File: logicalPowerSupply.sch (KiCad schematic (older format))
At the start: 12 parts

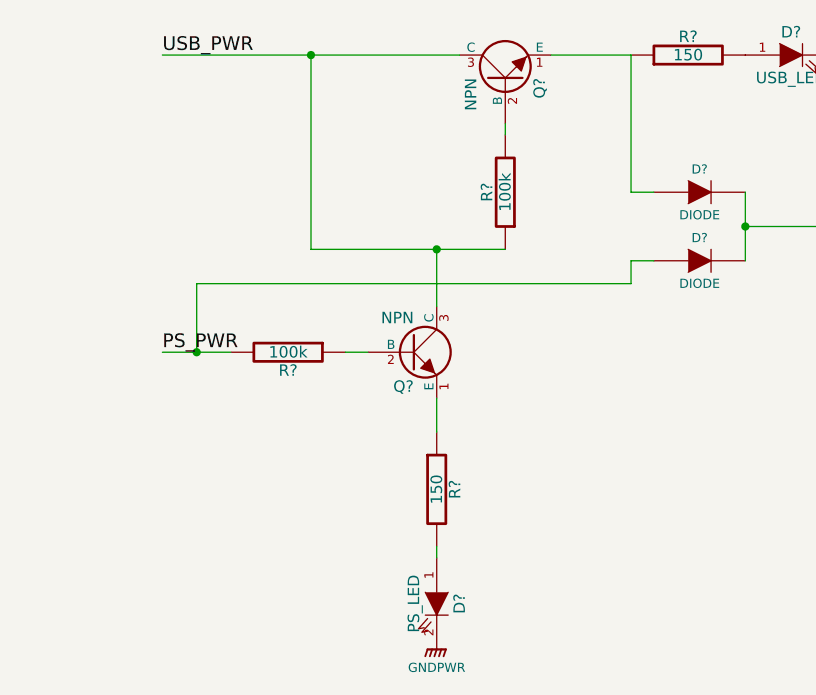
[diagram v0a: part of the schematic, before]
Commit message: Updating the logic circuit for the power supply
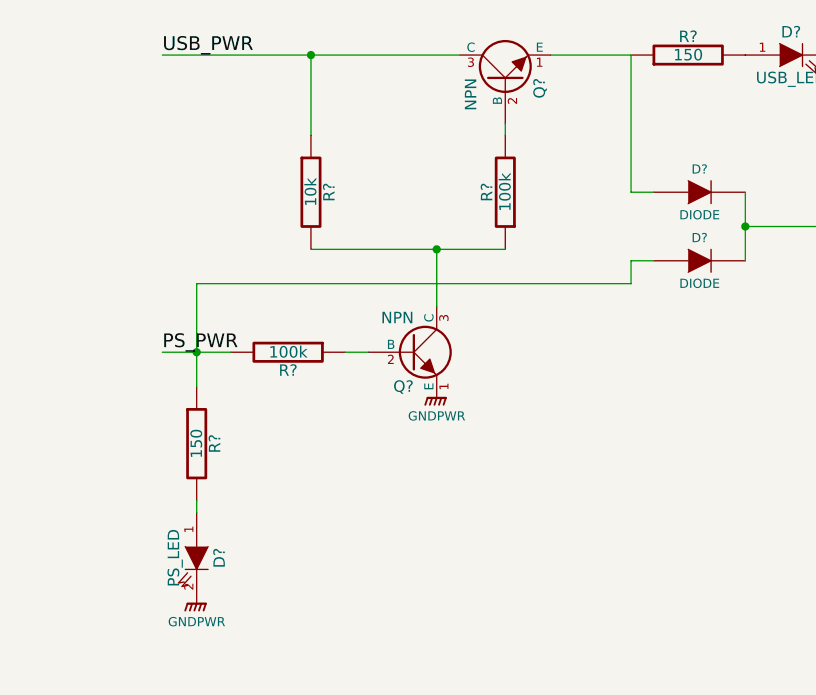
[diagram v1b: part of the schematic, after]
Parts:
- added R?: 10k, symbol R
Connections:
- net GNDPWR: now also Q?.1 (E)
- net PS_PWR: now also R?.1
- net USB_PWR: now also R?.1; no longer Q?.3 (C), R?.1
- new net: Q?.3 (C), R?.1, R?.2
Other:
- moved on the sheet: D?, R?
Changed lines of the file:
@@
-EESchema Schematic File Version 2  date 9/10/2011 2:20:11 AM
+EESchema Schematic File Version 2  date 9/12/2011 9:56:45 PM
 LIBS:power
 LIBS:device
@@
 LIBS:contrib
 LIBS:valves
+LIBS:logicalPowerSupply-cache
 EELAYER 25  0
 EELAYER END
@@
 Sheet 1 1
 Title ""
-Date "10 sep 2011"
+Date "13 sep 2011"
 Rev ""
 Comp ""
@@
 $Comp
 L GNDPWR #PWR?
+U 1 1 4E6EC664
+P 4050 2700
+F 0 "#PWR?" H 4050 2750 40  0001 C CNN
+F 1 "GNDPWR" H 4050 2620 40  0000 C CNN
+	1    4050 2700
+	1    0    0    -1
+$EndComp
+Wire Wire Line
+	3500 1200 3500 1550
+Connection ~ 3500 1200
+Wire Wire Line
+	2850 1200 4150 1200
+Wire Wire Line
+	5400 1800 5400 2100
+Wire Wire Line
+	5000 2100 4900 2100
+Wire Wire Line
+	3000 2200 4900 2200
+Connection ~ 3000 2500
+Wire Wire Line
+	3000 2200 3000 2500
+Wire Wire Line
+	2850 2500 3150 2500
+Wire Wire Line
+	4350 2050 3500 2050
+Wire Wire Line
+	3650 2500 3750 2500
+Wire Wire Line
+	4350 1500 4350 1550
+Wire Wire Line
+	4050 2300 4050 2050
+Connection ~ 4050 2050
+Wire Wire Line
+	4550 1200 4900 1200
+Wire Wire Line
+	4900 1200 4900 1800
+Wire Wire Line
+	4900 1800 5000 1800
+Wire Wire Line
+	4900 2200 4900 2100
+Wire Wire Line
+	5400 1950 6000 1950
+Connection ~ 5400 1950
+Wire Wire Line
+	3000 2650 3000 2500
+Wire Wire Line
+	3000 3150 3000 3200
+$Comp
+L R R?
+U 1 1 4E6EC640
+P 3500 1800
+F 0 "R?" V 3580 1800 50  0000 C CNN
+F 1 "10k" V 3500 1800 50  0000 C CNN
+	1    3500 1800
+	1    0    0    -1
+$EndComp
+$Comp
+L GNDPWR #PWR?
 U 1 1 4E6B0F6E
 P 5800 1200
@@
 	0    -1   -1   0
 $EndComp
-Wire Wire Line
-	4050 3350 4050 3400
-Wire Wire Line
-	4050 2850 4050 2700
-Connection ~ 5400 1950
-Wire Wire Line
-	5400 1950 6000 1950
-Wire Wire Line
-	4900 2200 4900 2100
-Wire Wire Line
-	5000 1800 4900 1800
-Wire Wire Line
-	4900 1800 4900 1200
-Wire Wire Line
-	4900 1200 4550 1200
-Connection ~ 4050 2050
-Wire Wire Line
-	4050 2300 4050 2050
-Wire Wire Line
-	4350 1500 4350 1550
-Wire Wire Line
-	3650 2500 3750 2500
-Wire Wire Line
-	4350 2050 3500 2050
-Wire Wire Line
-	2850 2500 3150 2500
-Wire Wire Line
-	3000 2500 3000 2200
-Connection ~ 3000 2500
-Wire Wire Line
-	3000 2200 4900 2200
-Wire Wire Line
-	4900 2100 5000 2100
-Wire Wire Line
-	5400 1800 5400 2100
-Wire Wire Line
-	2850 1200 4150 1200
-Connection ~ 3500 1200
-Wire Wire Line
-	3500 2050 3500 1200
 $Comp
 L LED D?
 U 1 1 4E6B0ED4
-P 4050 3600
-F 0 "D?" H 4050 3700 50  0000 C CNN
-F 1 "PS_LED" H 4050 3500 50  0000 C CNN
-	1    4050 3600
+P 3000 3400
+F 0 "D?" H 3000 3500 50  0000 C CNN
+F 1 "PS_LED" H 3000 3300 50  0000 C CNN
+	1    3000 3400
 	0    1    1    0
 $EndComp
@@
 L GNDPWR #PWR?
 U 1 1 4E6B01CF
-P 4050 3800
-F 0 "#PWR?" H 4050 3850 40  0001 C CNN
-F 1 "GNDPWR" H 4050 3720 40  0000 C CNN
-	1    4050 3800
+P 3000 3600
+F 0 "#PWR?" H 3000 3650 40  0001 C CNN
+F 1 "GNDPWR" H 3000 3520 40  0000 C CNN
+	1    3000 3600
 	1    0    0    -1
 $EndComp
@@
 L R R?
 U 1 1 4E6B0012
-P 4050 3100
-F 0 "R?" V 4130 3100 50  0000 C CNN
-F 1 "150" V 4050 3100 50  0000 C CNN
-	1    4050 3100
-	1    0    0    -1
-$EndComp
+P 3000 2900
+F 0 "R?" V 3080 2900 50  0000 C CNN
+F 1 "150" V 3000 2900 50  0000 C CNN
+	1    3000 2900
+	1    0    0    -1
+$EndComp

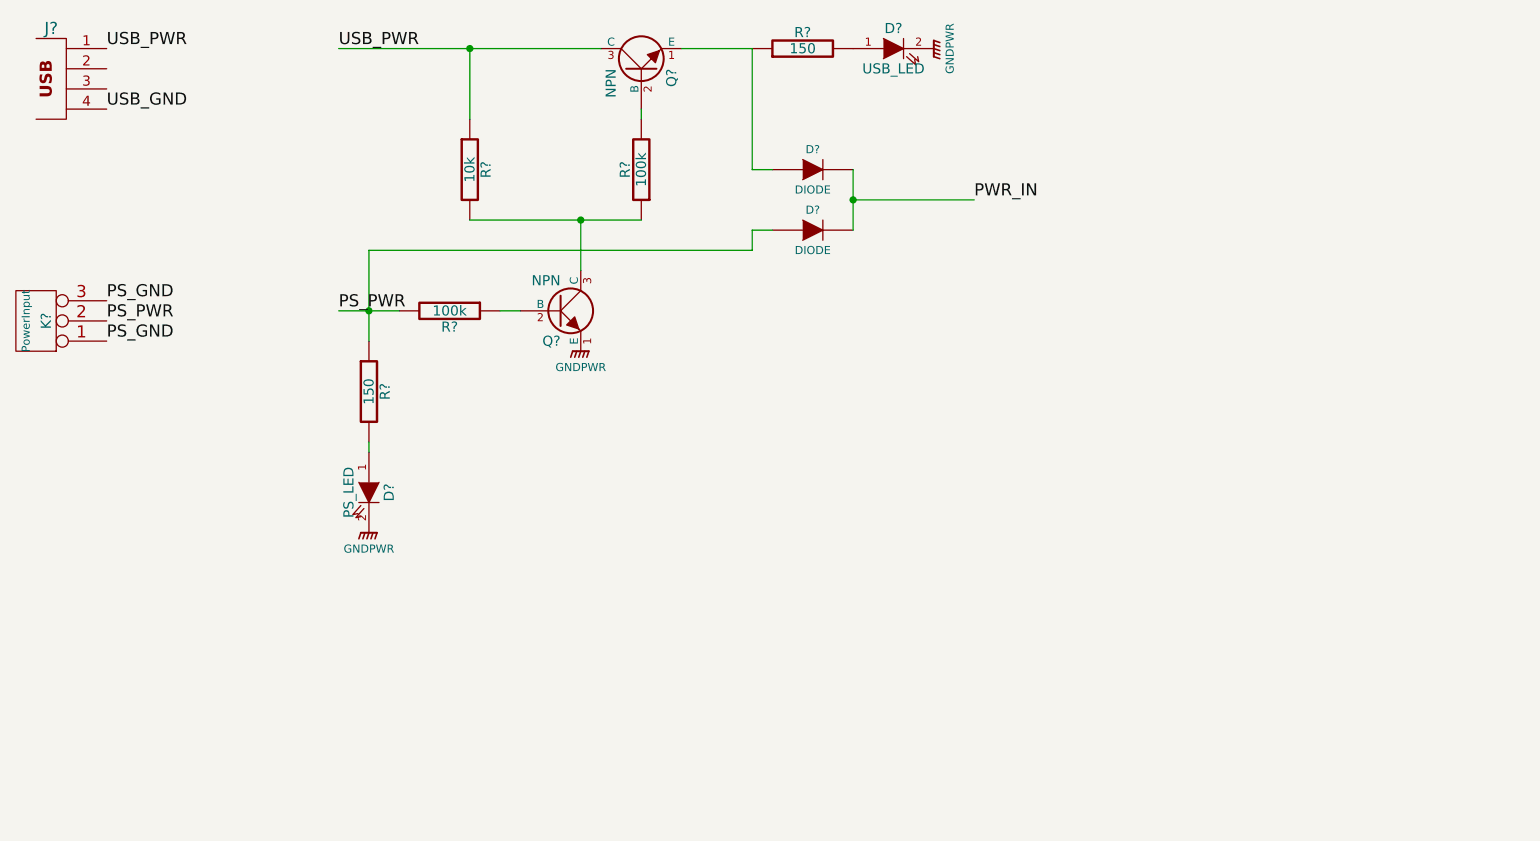
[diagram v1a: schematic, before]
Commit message: Added 3.3V switching Vreg to logPS schematic. Still need to settle on exact external components.
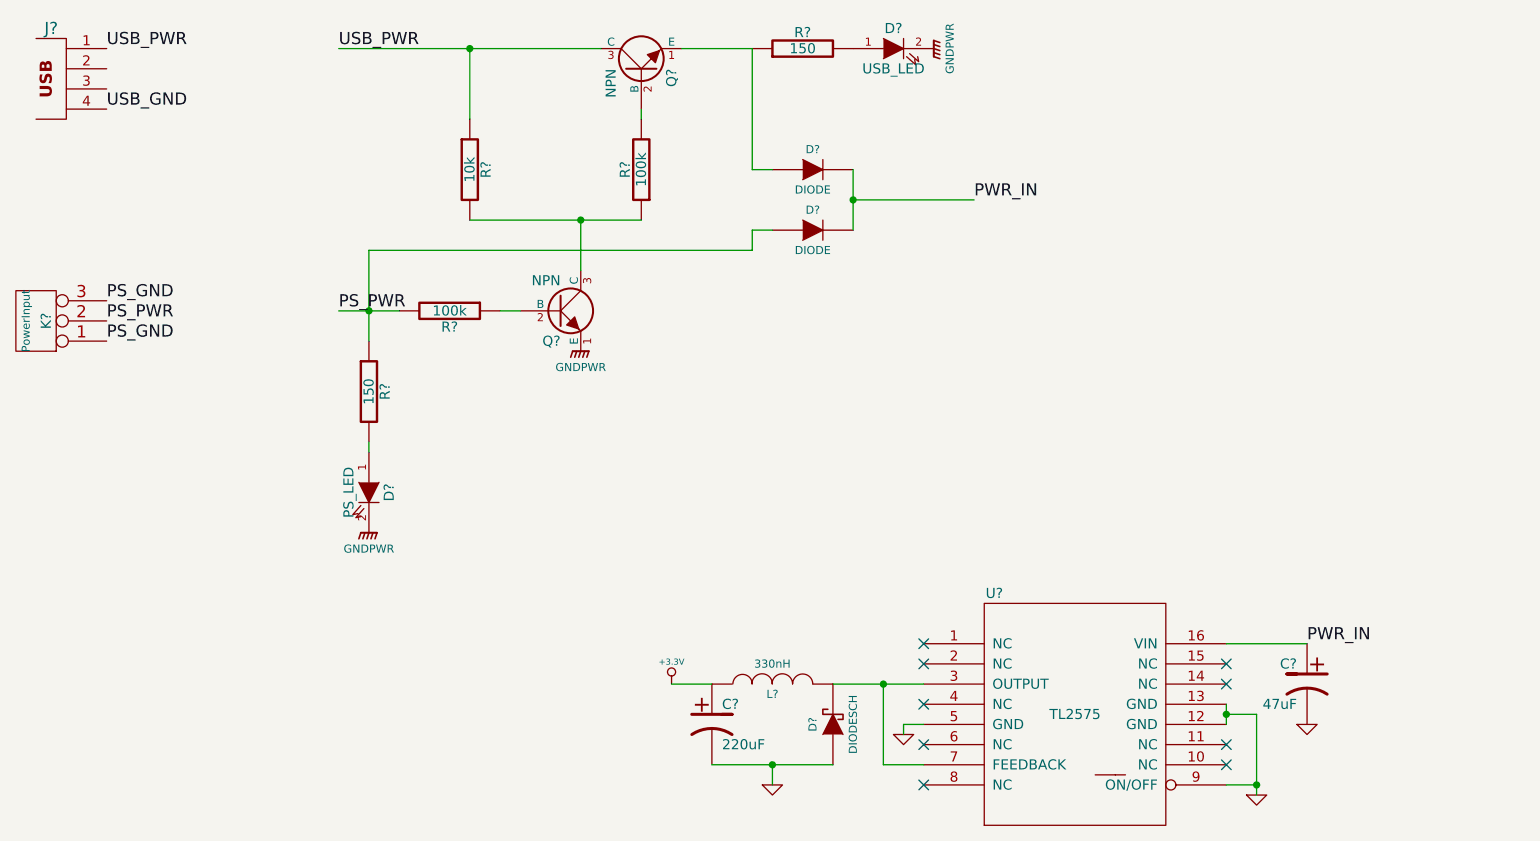
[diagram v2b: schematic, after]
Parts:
- added C?: 47uF, symbol CP1
- added C?: 220uF, symbol CP1
- added D?: DIODESCH, symbol DIODESCH
- added L?: 330nH, symbol INDUCTOR
- added U?: TL2575, symbol TL2575
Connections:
- net PWR_IN: now also C?.1, U?.16 (VIN)
- new net: D?.2 (K), L?.2, U?.3 (OUTPUT), U?.7 (FEEDBACK)
- new net +3.3V: C?.1, L?.1
- new net GND: C?.2, C?.2, D?.1 (A), U?.12 (GND), U?.13 (GND), U?.5 (GND), U?.9 (ON/OFF)
- no-connect marks 0 -> 9
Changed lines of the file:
@@
-EESchema Schematic File Version 2  date 9/12/2011 9:56:45 PM
+EESchema Schematic File Version 2  date 9/17/2011 1:18:32 AM
 LIBS:power
 LIBS:device
@@
 LIBS:contrib
 LIBS:valves
+LIBS:rrae
 LIBS:logicalPowerSupply-cache
 EELAYER 25  0
@@
 Sheet 1 1
 Title ""
-Date "13 sep 2011"
+Date "17 sep 2011"
 Rev ""
 Comp ""
@@
 Comment4 ""
 $EndDescr
+Wire Wire Line
+	4700 4350 4500 4350
+Wire Wire Line
+	5000 4850 5000 4750
+Connection ~ 5000 4750
+Wire Wire Line
+	7650 4150 7250 4150
+Connection ~ 7250 4500
+Wire Wire Line
+	7400 4900 7400 4500
+Wire Wire Line
+	7400 4500 7250 4500
+Wire Wire Line
+	5300 4350 5750 4350
+Wire Wire Line
+	7250 4450 7250 4550
+Wire Wire Line
+	3500 1200 3500 1550
+Connection ~ 3500 1200
+Wire Wire Line
+	2850 1200 4150 1200
+Wire Wire Line
+	5400 1800 5400 2100
+Wire Wire Line
+	5000 2100 4900 2100
+Wire Wire Line
+	4900 2200 3000 2200
+Connection ~ 3000 2500
+Wire Wire Line
+	2850 2500 3150 2500
+Wire Wire Line
+	4350 2050 3500 2050
+Wire Wire Line
+	3650 2500 3750 2500
+Wire Wire Line
+	4350 1500 4350 1550
+Wire Wire Line
+	4050 2300 4050 2050
+Connection ~ 4050 2050
+Wire Wire Line
+	4550 1200 4900 1200
+Wire Wire Line
+	4900 1200 4900 1800
+Wire Wire Line
+	4900 1800 5000 1800
+Wire Wire Line
+	4900 2200 4900 2100
+Wire Wire Line
+	5400 1950 6000 1950
+Connection ~ 5400 1950
+Wire Wire Line
+	3000 2200 3000 2650
+Wire Wire Line
+	3000 3150 3000 3200
+Wire Wire Line
+	5750 4550 5650 4550
+Wire Wire Line
+	5650 4550 5650 4600
+Wire Wire Line
+	5750 4750 5550 4750
+Wire Wire Line
+	5550 4750 5550 4350
+Connection ~ 5550 4350
+Wire Wire Line
+	7250 4850 7400 4850
+Connection ~ 7400 4850
+Wire Wire Line
+	5300 4750 4700 4750
+$Comp
+L GND #PWR?
+U 1 1 4E743AA5
+P 5000 4850
+F 0 "#PWR?" H 5000 4850 30  0001 C CNN
+F 1 "GND" H 5000 4780 30  0001 C CNN
+	1    5000 4850
+	1    0    0    -1
+$EndComp
+$Comp
+L INDUCTOR L?
+U 1 1 4E7439DF
+P 5000 4350
+F 0 "L?" V 4950 4350 40  0000 C CNN
+F 1 "330nH" V 5100 4350 40  0000 C CNN
+F 4 "Digi-Key" H 5000 4350 60  0001 C CNN "Supplier"
+F 5 "PCD1435CT-ND" H 5000 4350 60  0001 C CNN "PN"
+	1    5000 4350
+	0    -1   -1   0
+$EndComp
+$Comp
+L DIODESCH D?
+U 1 1 4E7437C8
+P 5300 4550
+F 0 "D?" H 5300 4650 40  0000 C CNN
+F 1 "DIODESCH" H 5300 4450 40  0000 C CNN
+F 4 "Digi-Key" H 5300 4550 60  0001 C CNN "Supplier"
+F 5 "568-4117-1-ND" H 5300 4550 60  0001 C CNN "PN"
+	1    5300 4550
+	0    -1   -1   0
+$EndComp
+$Comp
+L CP1 C?
+U 1 1 4E7435F7
+P 4700 4550
+F 0 "C?" H 4750 4650 50  0000 L CNN
+F 1 "220uF" H 4750 4450 50  0000 L CNN
+F 4 "Digi-Key" H 4700 4550 60  0001 C CNN "Supplier"
+F 5 "P5112-ND" H 4700 4550 60  0001 C CNN "PN"
+	1    4700 4550
+	1    0    0    -1
+$EndComp
+$Comp
+L GND #PWR?
+U 1 1 4E743381
+P 7650 4550
+F 0 "#PWR?" H 7650 4550 30  0001 C CNN
+F 1 "GND" H 7650 4480 30  0001 C CNN
+	1    7650 4550
+	1    0    0    -1
+$EndComp
+Text Label 7650 4150 0    60   ~ 0
+PWR_IN
+$Comp
+L CP1 C?
+U 1 1 4E7432CB
+P 7650 4350
+F 0 "C?" H 7700 4450 50  0000 L CNN
+F 1 "47uF" H 7700 4250 50  0000 L CNN
+F 4 "Digi-Key" H 7650 4350 60  0001 C CNN "Supplier"
+F 5 "493-1896-ND" H 7650 4350 60  0001 C CNN "PN"
+	1    7650 4350
+	-1   0    0    -1
+$EndComp
+$Comp
+L GND #PWR?
+U 1 1 4E742FEE
+P 5650 4600
+F 0 "#PWR?" H 5650 4600 30  0001 C CNN
+F 1 "GND" H 5650 4530 30  0001 C CNN
+	1    5650 4600
+	1    0    0    -1
+$EndComp
+$Comp
+L GND #PWR?
+U 1 1 4E742F8B
+P 7400 4900
+F 0 "#PWR?" H 7400 4900 30  0001 C CNN
+F 1 "GND" H 7400 4830 30  0001 C CNN
+	1    7400 4900
+	1    0    0    -1
+$EndComp
+$Comp
+L +3.3V #PWR?
+U 1 1 4E742F09
+P 4500 4350
+F 0 "#PWR?" H 4500 4310 30  0001 C CNN
+F 1 "+3.3V" H 4500 4460 30  0000 C CNN
+	1    4500 4350
+	1    0    0    -1
+$EndComp
+NoConn ~ 5750 4150
+NoConn ~ 5750 4250
+NoConn ~ 5750 4450
+NoConn ~ 5750 4650
+NoConn ~ 5750 4850
+NoConn ~ 7250 4750
+NoConn ~ 7250 4650
+NoConn ~ 7250 4350
+NoConn ~ 7250 4250
+$Comp
+L TL2575 U?
+U 1 1 4E742E92
+P 6500 4500
+F 0 "U?" H 6100 5100 50  0000 C CNN
+F 1 "TL2575" H 6500 4500 50  0000 C CNN
+	1    6500 4500
+	1    0    0    -1
+$EndComp
 $Comp
 L GNDPWR #PWR?
@@
 	1    0    0    -1
 $EndComp
-Wire Wire Line
-	3500 1200 3500 1550
-Connection ~ 3500 1200
-Wire Wire Line
-	2850 1200 4150 1200
-Wire Wire Line
-	5400 1800 5400 2100
-Wire Wire Line
-	5000 2100 4900 2100
-Wire Wire Line
-	3000 2200 4900 2200
-Connection ~ 3000 2500
-Wire Wire Line
-	3000 2200 3000 2500
-Wire Wire Line
-	2850 2500 3150 2500
-Wire Wire Line
-	4350 2050 3500 2050
-Wire Wire Line
-	3650 2500 3750 2500
-Wire Wire Line
-	4350 1500 4350 1550
-Wire Wire Line
-	4050 2300 4050 2050
-Connection ~ 4050 2050
-Wire Wire Line
-	4550 1200 4900 1200
-Wire Wire Line
-	4900 1200 4900 1800
-Wire Wire Line
-	4900 1800 5000 1800
-Wire Wire Line
-	4900 2200 4900 2100
-Wire Wire Line
-	5400 1950 6000 1950
-Connection ~ 5400 1950
-Wire Wire Line
-	3000 2650 3000 2500
-Wire Wire Line
-	3000 3150 3000 3200
 $Comp
 L R R?

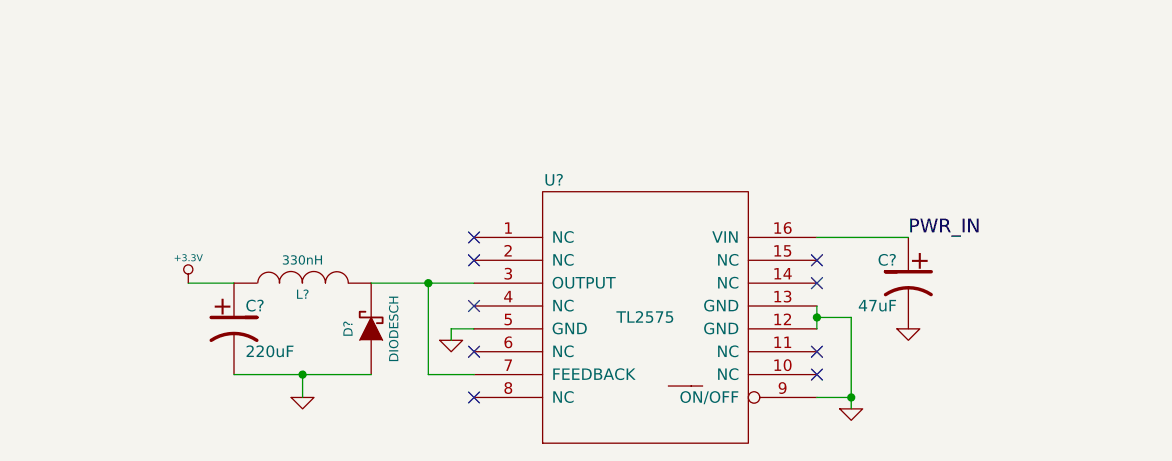
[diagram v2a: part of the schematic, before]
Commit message: Updated/corrected passive component values and product numbers per the TL2575 datasheet.
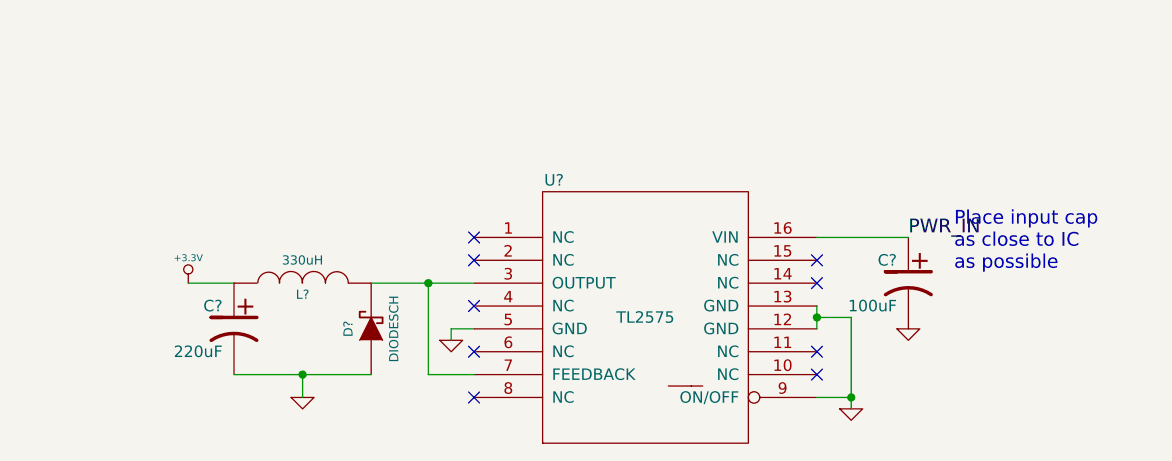
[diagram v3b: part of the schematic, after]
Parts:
- C?: value 47uF -> 100uF; PN 493-1896-ND -> P5165-ND
- D?: PN 568-4117-1-ND -> B340A-FDICT-ND
- L?: value 330nH -> 330uH; PN PCD1435CT-ND -> SRR1260-331KCT-ND
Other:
- note added: "Place input cap \nas close to IC \nas possible"
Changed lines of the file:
@@
-EESchema Schematic File Version 2  date 9/17/2011 1:18:32 AM
+EESchema Schematic File Version 2  date 9/20/2011 9:07:33 PM
 LIBS:power
 LIBS:device
@@
 LIBS:contrib
 LIBS:valves
-LIBS:rrae
 LIBS:logicalPowerSupply-cache
 EELAYER 25  0
@@
 Sheet 1 1
 Title ""
-Date "17 sep 2011"
+Date "21 sep 2011"
 Rev ""
 Comp ""
@@
 Comment4 ""
 $EndDescr
+Text Notes 7850 4300 0    60   ~ 0
+Place input cap \nas close to IC \nas possible
 Wire Wire Line
 	4700 4350 4500 4350
@@
 P 5000 4350
 F 0 "L?" V 4950 4350 40  0000 C CNN
-F 1 "330nH" V 5100 4350 40  0000 C CNN
+F 1 "330uH" V 5100 4350 40  0000 C CNN
 F 4 "Digi-Key" H 5000 4350 60  0001 C CNN "Supplier"
-F 5 "PCD1435CT-ND" H 5000 4350 60  0001 C CNN "PN"
+F 5 "SRR1260-331KCT-ND" H 5000 4350 60  0001 C CNN "PN"
 	1    5000 4350
 	0    -1   -1   0
@@
 F 1 "DIODESCH" H 5300 4450 40  0000 C CNN
 F 4 "Digi-Key" H 5300 4550 60  0001 C CNN "Supplier"
-F 5 "568-4117-1-ND" H 5300 4550 60  0001 C CNN "PN"
+F 5 "B340A-FDICT-ND" H 5300 4550 60  0001 C CNN "PN"
 	1    5300 4550
 	0    -1   -1   0
@@
 F 5 "P5112-ND" H 4700 4550 60  0001 C CNN "PN"
 	1    4700 4550
-	1    0    0    -1
+	-1   0    0    -1
 $EndComp
 $Comp
@@
 P 7650 4350
 F 0 "C?" H 7700 4450 50  0000 L CNN
-F 1 "47uF" H 7700 4250 50  0000 L CNN
+F 1 "100uF" H 7700 4250 50  0000 L CNN
 F 4 "Digi-Key" H 7650 4350 60  0001 C CNN "Supplier"
-F 5 "493-1896-ND" H 7650 4350 60  0001 C CNN "PN"
+F 5 "P5165-ND" H 7650 4350 60  0001 C CNN "PN"
 	1    7650 4350
 	-1   0    0    -1
